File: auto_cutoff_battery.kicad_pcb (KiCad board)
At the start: 2 copper layers, 100 x 50 mm, 0 parts

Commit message: started PCB design
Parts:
- added BAT1: Conn_01x02_Socket, Connector_PinSocket_2.54mm:PinSocket_1x02_P2.54mm_Vertical, F.Cu at (196.2, 94.6)
- added D1: 1N5408, Diode_THT:D_DO-201AD_P15.24mm_Horizontal, F.Cu at (181.4, 106.7)
- added D2: 1N5408, Diode_THT:D_DO-201AD_P15.24mm_Horizontal, F.Cu at (180.0, 64.5)
- added H1: MountingHole, MountingHole:MountingHole_3.2mm_M3_ISO7380_Pad, F.Cu at (105.0, 84.2)
- added H2: MountingHole, MountingHole:MountingHole_3.2mm_M3_ISO7380_Pad, F.Cu at (104.6, 105.2)
- added H3: MountingHole, MountingHole:MountingHole_3.2mm_M3_ISO7380_Pad, F.Cu at (195.2, 84.7)
- added H4: MountingHole, MountingHole:MountingHole_3.2mm_M3_ISO7380_Pad, F.Cu at (195.8, 105.3)
- added IN_OUT1: Conn_02x03_Counter_Clockwise, Connector_PinSocket_2.54mm:PinSocket_2x03_P2.54mm_Vertical, F.Cu at (105.9, 92.6)
- added Q1: IRF540N, Package_TO_SOT_THT:TO-220-3_Vertical, F.Cu at (184.2, 100.6)
- added Q10: S8050, Package_TO_SOT_THT:TO-92_Inline_Wide, F.Cu at (150.1, 103.8)
- added Q2: IRF9540N, Package_TO_SOT_THT:TO-220-3_Vertical, F.Cu at (183.1, 75.3)
- added Q3: S8050, Package_TO_SOT_THT:TO-92_Inline_Wide, F.Cu at (121.8, 97.6)
- added Q4: S8050, Package_TO_SOT_THT:TO-92_Inline_Wide, F.Cu at (121.9, 66.2)
- added Q5: S8050, Package_TO_SOT_THT:TO-92_Inline_Wide, F.Cu at (143.0, 77.2)
- added Q6: S8050, Package_TO_SOT_THT:TO-92_Inline_Wide, F.Cu at (148.2, 77.4)
- added Q7: S8050, Package_TO_SOT_THT:TO-92_Inline_Wide, F.Cu at (144.0, 95.3)
- added Q8: S8050, Package_TO_SOT_THT:TO-92_Inline_Wide, F.Cu at (144.1, 102.8)
- added Q9: S8050, Package_TO_SOT_THT:TO-92_Inline_Wide, F.Cu at (153.3, 77.5)
- added R1: R, Resistor_THT:R_Axial_DIN0207_L6.3mm_D2.5mm_P7.62mm_Horizontal, F.Cu at (119.4, 102.1)
- added R12: R, Resistor_THT:R_Axial_DIN0207_L6.3mm_D2.5mm_P7.62mm_Horizontal, F.Cu at (119.8, 80.5)
- added R13: R, Resistor_THT:R_Axial_DIN0207_L6.3mm_D2.5mm_P7.62mm_Horizontal, F.Cu at (127.5, 102.1)
- added R14: R, Resistor_THT:R_Axial_DIN0207_L6.3mm_D2.5mm_P7.62mm_Horizontal, F.Cu at (119.3, 97.5)
- added R15: R, Resistor_THT:R_Axial_DIN0207_L6.3mm_D2.5mm_P7.62mm_Horizontal, F.Cu at (112.3, 73.3)
- added R16: R, Resistor_THT:R_Axial_DIN0207_L6.3mm_D2.5mm_P7.62mm_Horizontal, F.Cu at (127.9, 73.8)
- added R17: R, Resistor_THT:R_Axial_DIN0207_L6.3mm_D2.5mm_P7.62mm_Horizontal, F.Cu at (112.3, 70.2)
- added R18: R, Resistor_THT:R_Axial_DIN0207_L6.3mm_D2.5mm_P7.62mm_Horizontal, F.Cu at (127.9, 70.3)
- added R19: R, Resistor_THT:R_Axial_DIN0207_L6.3mm_D2.5mm_P7.62mm_Horizontal, F.Cu at (119.2, 66.1)
- added R2: R, Resistor_THT:R_Axial_DIN0207_L6.3mm_D2.5mm_P7.62mm_Horizontal, F.Cu at (119.5, 105.5)
- added R20: R, Resistor_THT:R_Axial_DIN0207_L6.3mm_D2.5mm_P7.62mm_Horizontal, F.Cu at (144.7, 70.0)
- added R21: R, Resistor_THT:R_Axial_DIN0207_L6.3mm_D2.5mm_P7.62mm_Horizontal, F.Cu at (144.7, 74.0)
- added R22: R, Resistor_THT:R_Axial_DIN0207_L6.3mm_D2.5mm_P7.62mm_Horizontal, F.Cu at (148.1, 96.0)
- added R23: R, Resistor_THT:R_Axial_DIN0207_L6.3mm_D2.5mm_P7.62mm_Horizontal, F.Cu at (152.1, 96.0)
- added R3: R, Resistor_THT:R_Axial_DIN0207_L6.3mm_D2.5mm_P7.62mm_Horizontal, F.Cu at (172.3, 68.9)
- added R4: R, Resistor_THT:R_Axial_DIN0207_L6.3mm_D2.5mm_P7.62mm_Horizontal, F.Cu at (162.3, 71.5)
- added R5: R, Resistor_THT:R_Axial_DIN0207_L6.3mm_D2.5mm_P7.62mm_Horizontal, F.Cu at (162.8, 76.6)
- added R6: R, Resistor_THT:R_Axial_DIN0207_L6.3mm_D2.5mm_P7.62mm_Horizontal, F.Cu at (178.9, 102.1)
- added R7: R, Resistor_THT:R_Axial_DIN0207_L6.3mm_D2.5mm_P7.62mm_Horizontal, F.Cu at (164.6, 95.1)
- added R8: R, Resistor_THT:R_Axial_DIN0207_L6.3mm_D2.5mm_P7.62mm_Horizontal, F.Cu at (116.7, 89.0)
- added R9: R, Resistor_THT:R_Axial_DIN0207_L6.3mm_D2.5mm_P7.62mm_Horizontal, F.Cu at (134.7, 105.8)
- added U1: TL431LP, Package_TO_SOT_THT:TO-92_Inline_Wide, F.Cu at (123.6, 106.4)
- added U2: PC817, Package_DIP:DIP-4_W7.62mm, F.Cu at (120.2, 83.7)
- added U3: PC817, Package_DIP:DIP-4_W7.62mm, F.Cu at (167.6, 96.8)
- added U4: PC817, Package_DIP:DIP-4_W7.62mm, F.Cu at (172.4, 72.6)
- added U5: TL431LP, Package_TO_SOT_THT:TO-92_Inline_Wide, F.Cu at (124.2, 74.6)

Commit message: finished PCB solution
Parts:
- removed BAT1: Conn_01x02_Socket, Connector_PinSocket_2.54mm:PinSocket_1x02_P2.54mm_Vertical
- added Bridge1: R, Resistor_THT:R_Axial_DIN0207_L6.3mm_D2.5mm_P5.08mm_Vertical, F.Cu at (151.9, 105.0)
- added Bridge2: R, Resistor_THT:R_Axial_DIN0207_L6.3mm_D2.5mm_P5.08mm_Vertical, F.Cu at (139.1, 82.1)
- added Bridge3: R, Resistor_THT:R_Axial_DIN0207_L6.3mm_D2.5mm_P5.08mm_Vertical, F.Cu at (192.7, 76.8)
- added Bridge4: R, Resistor_THT:R_Axial_DIN0207_L6.3mm_D2.5mm_P15.24mm_Horizontal, F.Cu at (164.8, 108.6)
- added D3: RED_LED, LED_THT:LED_D3.0mm, F.Cu at (167.3, 48.0)
- added D4: GREEN_LED, LED_THT:LED_D3.0mm, F.Cu at (167.3, 53.5)
- added J3: Conn_01x01_Socket, Connector_PinSocket_2.54mm:PinSocket_1x01_P2.54mm_Vertical, F.Cu at (199.2, 69.5)
- added J4: Conn_01x01_Socket, Connector_PinSocket_2.54mm:PinSocket_1x01_P2.54mm_Vertical, F.Cu at (196.4, 98.2)
- added R10: R, Resistor_THT:R_Axial_DIN0207_L6.3mm_D2.5mm_P7.62mm_Horizontal, F.Cu at (172.9, 54.4)
- added R11: R, Resistor_THT:R_Axial_DIN0207_L6.3mm_D2.5mm_P7.62mm_Horizontal, F.Cu at (173.1, 51.2)
- moved R2 39.2 mm to (119.0, 66.3), turned to -90 degrees
- moved R1 37.1 mm to (129.2, 66.3)
- moved R9 37.0 mm to (116.0, 73.9), turned to 90 degrees
- moved Q4 36.9 mm to (134.7, 100.8), turned to 180 degrees
- moved R18 34.3 mm to (127.9, 104.6)
- moved R19 34.0 mm to (132.3, 97.5), turned to 0 degrees
- moved R14 33.5 mm to (131.4, 66.2), turned to 0 degrees
- moved R16 33.2 mm to (116.8, 105.1), turned to 90 degrees
- moved U1 32.4 mm to (123.3, 74.0)
- moved U5 30.5 mm to (124.1, 105.1)
- moved R17 30.3 mm to (129.9, 94.9), turned to 180 degrees
- moved Q3 29.6 mm to (131.8, 69.8), turned to 180 degrees
- moved R13 28.6 mm to (126.4, 73.5)
- moved R21 27.4 mm to (162.7, 94.7), turned to 180 degrees
- moved Q6 26.2 mm to (156.2, 102.3), turned to 90 degrees
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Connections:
- IN_OUT1 pad 5: unconnected-(IN_OUT1-Pin_5-Pad5) -> IN_OUT-
- IN_OUT1 pad 6: unconnected-(IN_OUT1-Pin_6-Pad6) -> IN_OUT+
- Q5 pad 2: Net-(Q4-C) -> Net-(Q5-B)
- Q8 pad 2: Net-(Q6-B) -> Net-(Q5-B)
- R12 pad 2: Net-(Q6-B) -> Net-(Q5-B)
- R4 pad 2: +5V -> BAT+
- U2 pad 4: Net-(Q6-B) -> Net-(Q5-B)
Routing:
- net BAT+: track 0.00 -> 365.9 mm
- net BAT-: track 0.00 -> 339.7 mm
- net IN_OUT-: track 0.00 -> 221.0 mm
- net IN_OUT+: track 0.00 -> 186.4 mm
- net Net-(Q5-B): track 0.00 -> 49.6 mm
- net Net-(Q4-C): track 0.00 -> 27.7 mm
- net Net-(Q3-C): track 0.00 -> 27.6 mm
- net Net-(Q5-C): track 0.00 -> 17.8 mm
- net PMOS_CONTROL: track 0.00 -> 15.4 mm
- net Net-(Q10-B): track 0.00 -> 14.5 mm
- net Net-(U5-K): track 0.00 -> 12.0 mm
- net not NMOS_CONTROL: track 0.00 -> 11.9 mm
- net Net-(Q1-G): track 0.00 -> 10.8 mm
- net Net-(U1-K): track 0.00 -> 9.22 mm
- net Net-(Q2-G): track 0.00 -> 8.74 mm
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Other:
- board size 100 x 50 mm -> 100 x 52.1 mm

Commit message: finished PCB and added gcode files
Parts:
- removed D3: RED_LED, LED_THT:LED_D3.0mm
- removed D4: GREEN_LED, LED_THT:LED_D3.0mm
- removed IN_OUT1: Conn_02x03_Counter_Clockwise, Connector_PinSocket_2.54mm:PinSocket_2x03_P2.54mm_Vertical
- removed R10, R11: R, Resistor_THT:R_Axial_DIN0207_L6.3mm_D2.5mm_P7.62mm_Horizontal
- added J1: RJ45, Connector_RJ:RJ45_Molex_0855135013_Vertical, F.Cu at (58.7, 59.0)
- added J5: Conn_01x03_Socket, Connector_Wire:SolderWire-0.1sqmm_1x03_P3.6mm_D0.4mm_OD1mm, F.Cu at (66.4, 91.2)
- added J6: Conn_01x03_Socket, Connector_Wire:SolderWire-0.1sqmm_1x03_P3.6mm_D0.4mm_OD1mm, F.Cu at (73.6, 87.9)
- Bridge4: footprint Resistor_THT:R_Axial_DIN0207_L6.3mm_D2.5mm_P15.24mm_Horizontal -> Resistor_THT:R_Axial_DIN0207_L6.3mm_D2.5mm_P7.62mm_Horizontal
- H1, H2, H3, H4: footprint MountingHole:MountingHole_3.2mm_M3_ISO7380_Pad -> MountingHole:MountingHole_5.3mm_M5_DIN965_Pad
- moved D2 77.8 mm to (110.8, 71.0), turned to 0 degrees
- moved D1 68.0 mm to (117.8, 76.8), turned to 0 degrees
- moved J4 64.3 mm to (141.6, 64.7)
- moved Bridge3 62.6 mm to (130.3, 72.0)
- moved J3 62.6 mm to (136.7, 64.7)
- moved Q2 62.6 mm to (129.6, 60.3)
- moved R3 62.6 mm to (126.4, 67.0)
- moved U4 62.6 mm to (116.0, 63.3)
- moved R4 62.2 mm to (113.6, 63.0)
- moved R5 62.2 mm to (113.6, 66.0)
- moved H4 58.7 mm to (144.0, 94.0)
- moved H3 57.7 mm to (144.0, 75.0), turned to 0 degrees
- moved Bridge4 55.7 mm to (114.6, 84.2), turned to -90 degrees
- moved H1 55.5 mm to (56.0, 75.0)
- moved H2 54.4 mm to (56.0, 94.0)
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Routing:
- net BAT+: track 365.9 -> 210.7 mm
- net BAT-: track 339.7 -> 244.1 mm
- net IN_OUT+: track 186.4 -> 136.1 mm
- net IN_OUT-: track 221.0 -> 179.6 mm
- net Net-(Q3-C): track 27.6 -> 15.9 mm
- net Net-(Q5-B): track 49.6 -> 38.5 mm
- net PMOS_CONTROL: track 15.4 -> 8.26 mm
- net Net-(D3-A): track 4.65 -> 0.00 mm
- net Net-(D4-A): track 3.45 -> 0.00 mm
- net Net-(U5-K): track 12.0 -> 14.6 mm
- net Net-(Q4-C): track 27.7 -> 25.7 mm
- net Net-(R8-Pad2): track 4.60 -> 5.55 mm
- net Net-(Q4-B): track 6.31 -> 6.99 mm
- net Net-(Q5-C): track 17.8 -> 17.2 mm
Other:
- board size 100 x 52.1 mm -> 100 x 52 mm

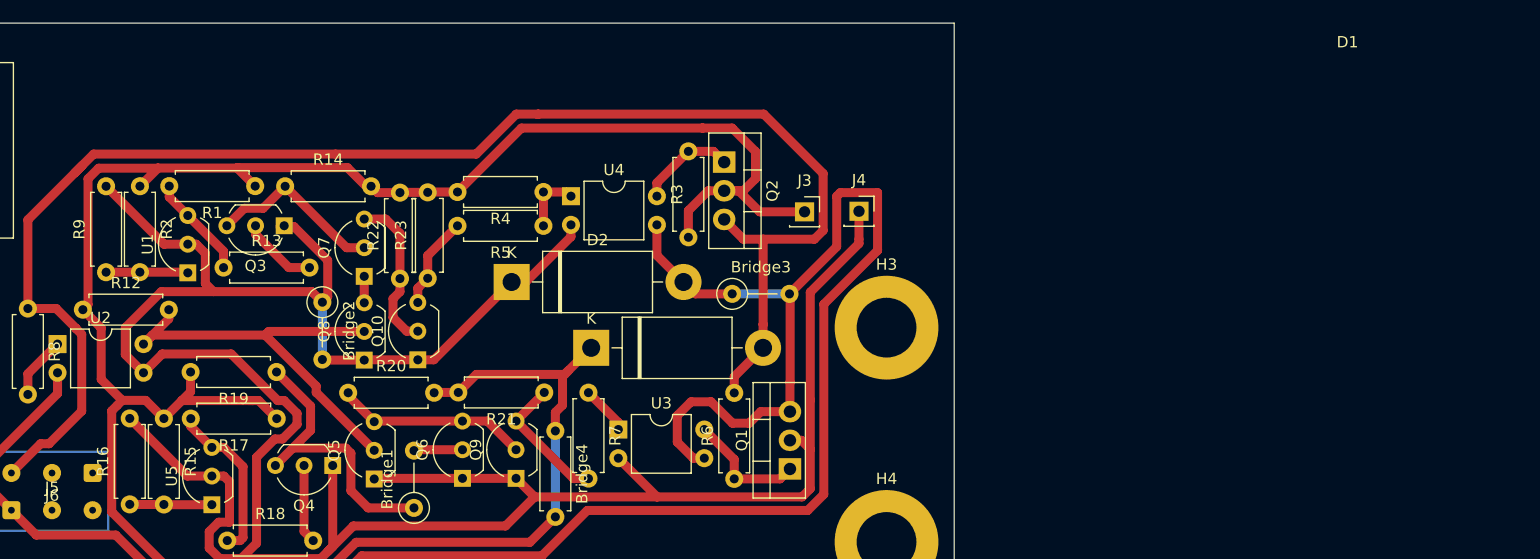
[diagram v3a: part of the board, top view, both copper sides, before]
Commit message: added resistor values
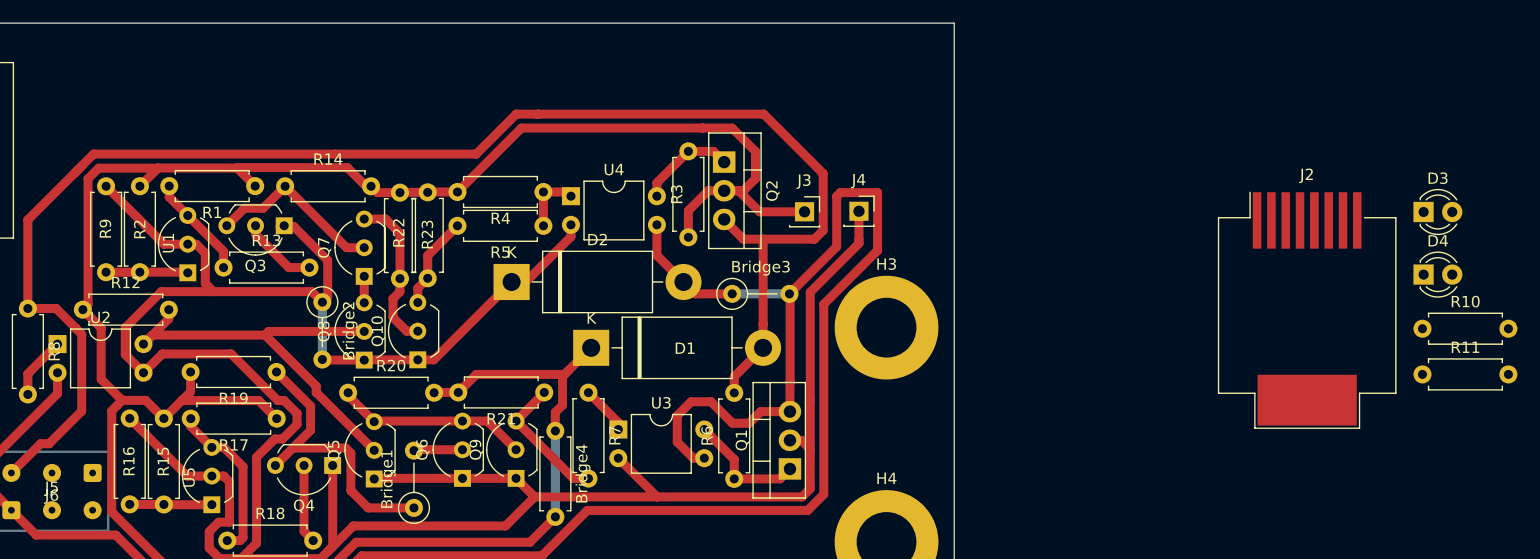
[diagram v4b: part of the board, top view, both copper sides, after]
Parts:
- added D3: RED_LED, LED_THT:LED_D3.0mm, F.Cu at (191.6, 64.7)
- added D4: YELLOW_LED, LED_THT:LED_D3.0mm, F.Cu at (191.6, 70.3)
- added J2: RJ45, Connector_RJ:RJ45_Molex_0855135013_Vertical, F.Cu at (181.3, 73.3)
- added R10: R, Resistor_THT:R_Axial_DIN0207_L6.3mm_D2.5mm_P7.62mm_Horizontal, F.Cu at (191.5, 75.1)
- added R11: R, Resistor_THT:R_Axial_DIN0207_L6.3mm_D2.5mm_P7.62mm_Horizontal, F.Cu at (191.5, 79.1)
- R1, R14, R17, R19, R6: value R -> 2k
- R12: value R -> 470
- R13, R18: value R -> 200k
- R15: value R -> 5k
- R16: value R -> 1.2k
- R20, R21, R22, R23: value R -> 680
- R3, R7, R8: value R -> 1k
- R5: value R -> 220
